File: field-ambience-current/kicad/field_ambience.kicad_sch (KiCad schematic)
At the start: 0 parts

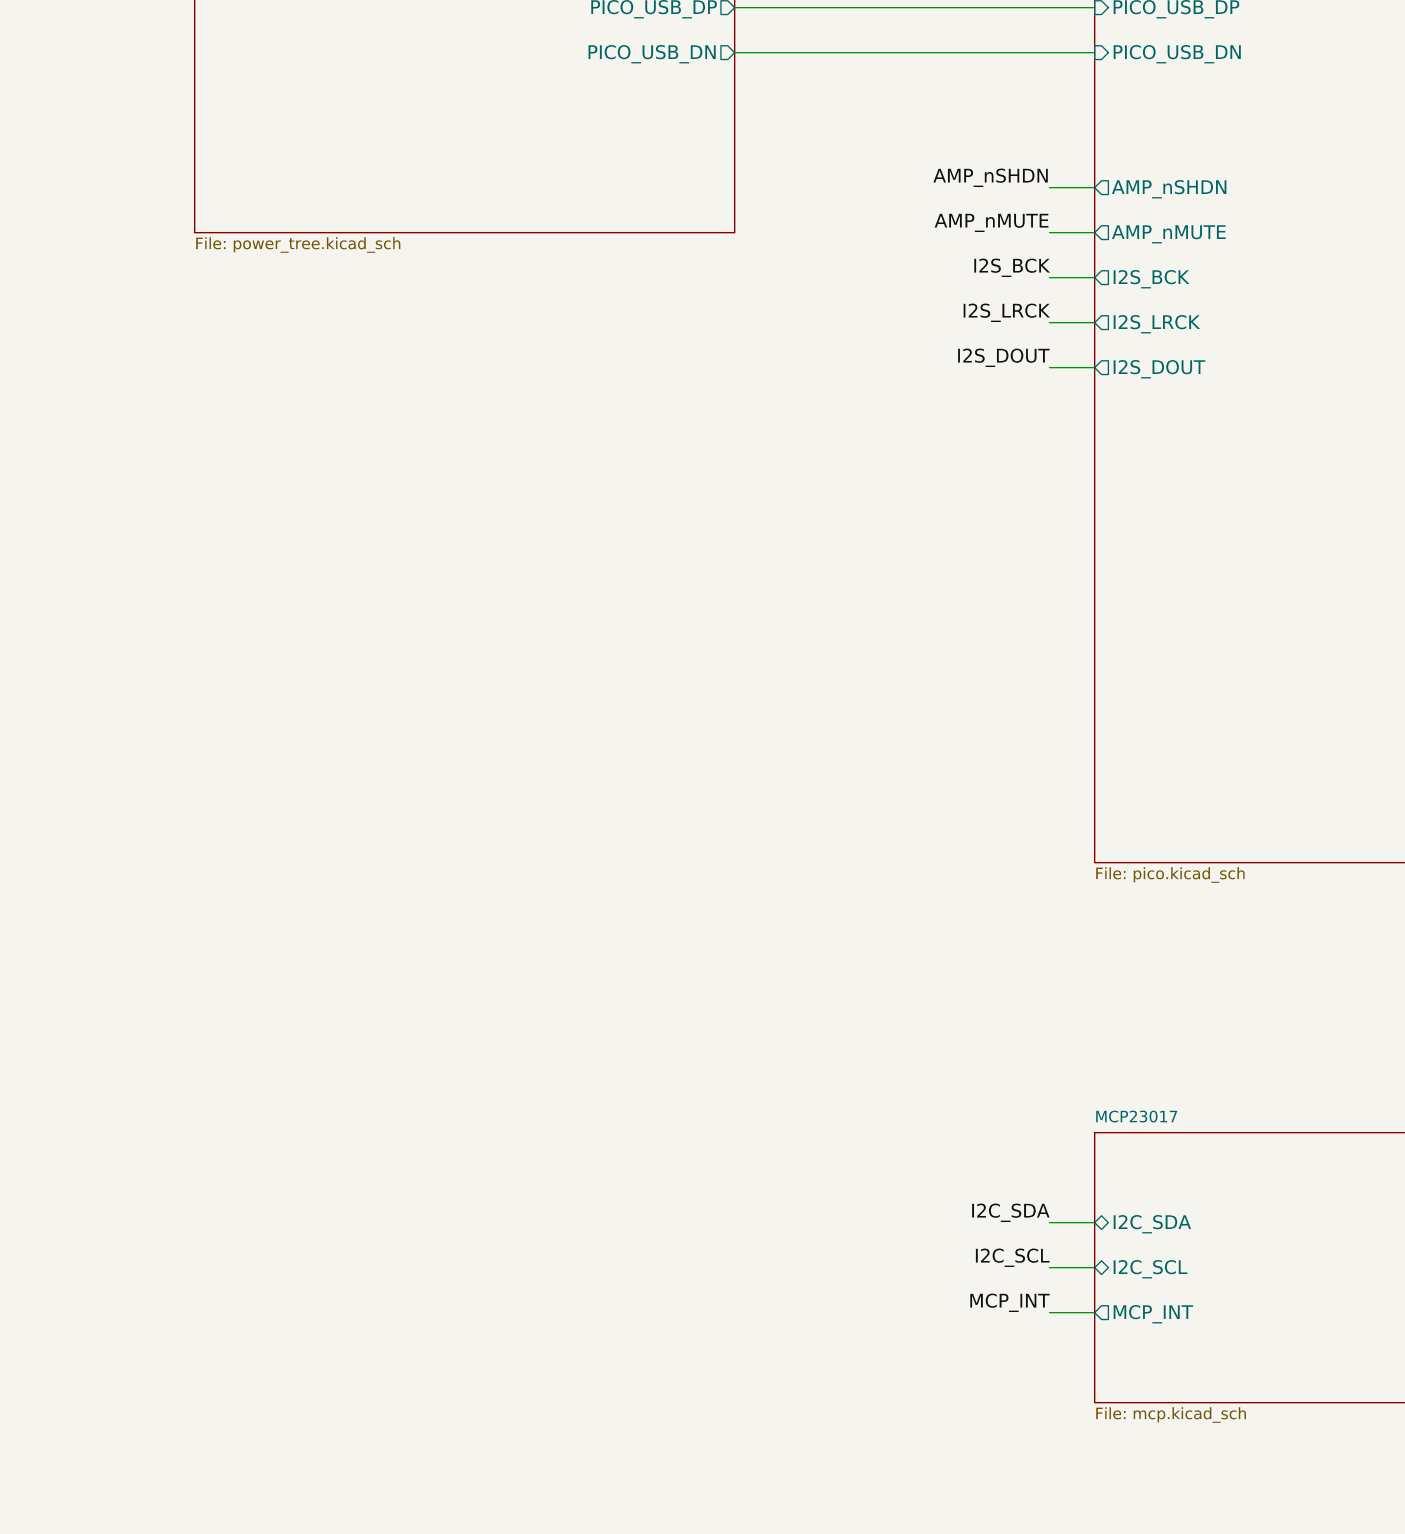
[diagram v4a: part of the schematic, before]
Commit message: pcb(gen): r12-Sense + r9-Battery — KiCad-Generator vervollständigt
Zweite + dritte Hälfte von r10-B9/r7-B3. Bringt Generator vollständig in
Sync mit allen SPEC-Revisionen r9 (Battery-Add), r12 (Battery-Sense-HW),
r10-LED (LED1 auf PCA-Ch 10).

5 neue Library-Symbole (zwischen _pca9685pw_lib_symbol und
_rotary_encoder_switch_lib_symbol):
- _mcp73831_lib_symbol() — SOT-23-5, 5-pin Microchip-Charger
- _tps61089_lib_symbol() — QFN-12+ePAD, 13-pin TI-Boost
- _dmg2305ux_lib_symbol() — SOT-23, 3-pin P-MOSFET
- _inductor_lib_symbol() — Device:L, 2-pin
- _schottky_diode_lib_symbol() — Device:D_Schottky, 2-pin

Neuer Sheet 7 battery.kicad_sch (106 KB, 1848 Zeilen, paren-balanced):
- U7 MCP73831 LiPo-Charger 500mA via R21=2kΩ R_PROG, STAT→R_CHRG→LED_CHRG→+5V
- U8 TPS61089 Boost LiPo→5V mit L1 2.2µH + R23/R24 FB-Divider (200k/39k → ~4.92V)
- Q1 DMG2305UX P-MOS Power-Path (S=VBUS_USBC, D=+5V_OUT, G→R22 10kΩ pull-down)
- D3 SS34 Schottky zwischen BOOST_OUT und +5V_OUT (Reverse-Protect)
- J9 JST-PH-2P, C_BAT_IN/HF (22µF+100nF), C_BOOST_OUT/HF (22µF+100nF)
- Hier-I/O: VBUS_USBC ← (Power-Tree), BAT_PLUS → (Pico), +5V_OUT → (System-Rail)

r12-Sense in pico_sheet:
- GP26 STATUS_LED-Block entfernt (R19+LED1+GND-Flag weg, 0 hits in pico.kicad_sch)
- BAT_SENSE-Divider rein: R_BAT_DIV_TOP/BOT (100kΩ je), C_BAT_FILT (10nF)
- Hier-Input BAT_PLUS am Divider-Top

r12-Sense in mcp_sheet:
- GPA7 NC_GPA7 → USB_VBUS_SENSE mit R_VBUS_SENSE (10kΩ Series) + R_VBUS_PD
  (100kΩ Pull-Down) + hier-Input VBUS_USBC
- LED1 + R_LED_STATUS (390Ω 0603) auf PCA-Ch 10 (Pin 17, rechts) bei (130, 230)
- STATUS_LED_K Net-Label matched LED1-Kathode mit PCA-LED10-Pin
- NC-Loop reduziert auf LED11-LED15

power_tree_sheet:
- VBUS_USBC hier-Output (90° nach oben) am pre-fuse Rail-Tap bei (30.48, RAIL_Y-6)

root_sheet:
- Sheet 7 Battery-Block bei (30, 180) size 60×40 mit Pins VBUS_USBC/BAT_PLUS/+5V_OUT
- Existing Sheet-Blöcke erweitert: power_tree +VBUS_USBC out (90,95), pico +BAT_PLUS
  in (130,165), mcp +VBUS_USBC in 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
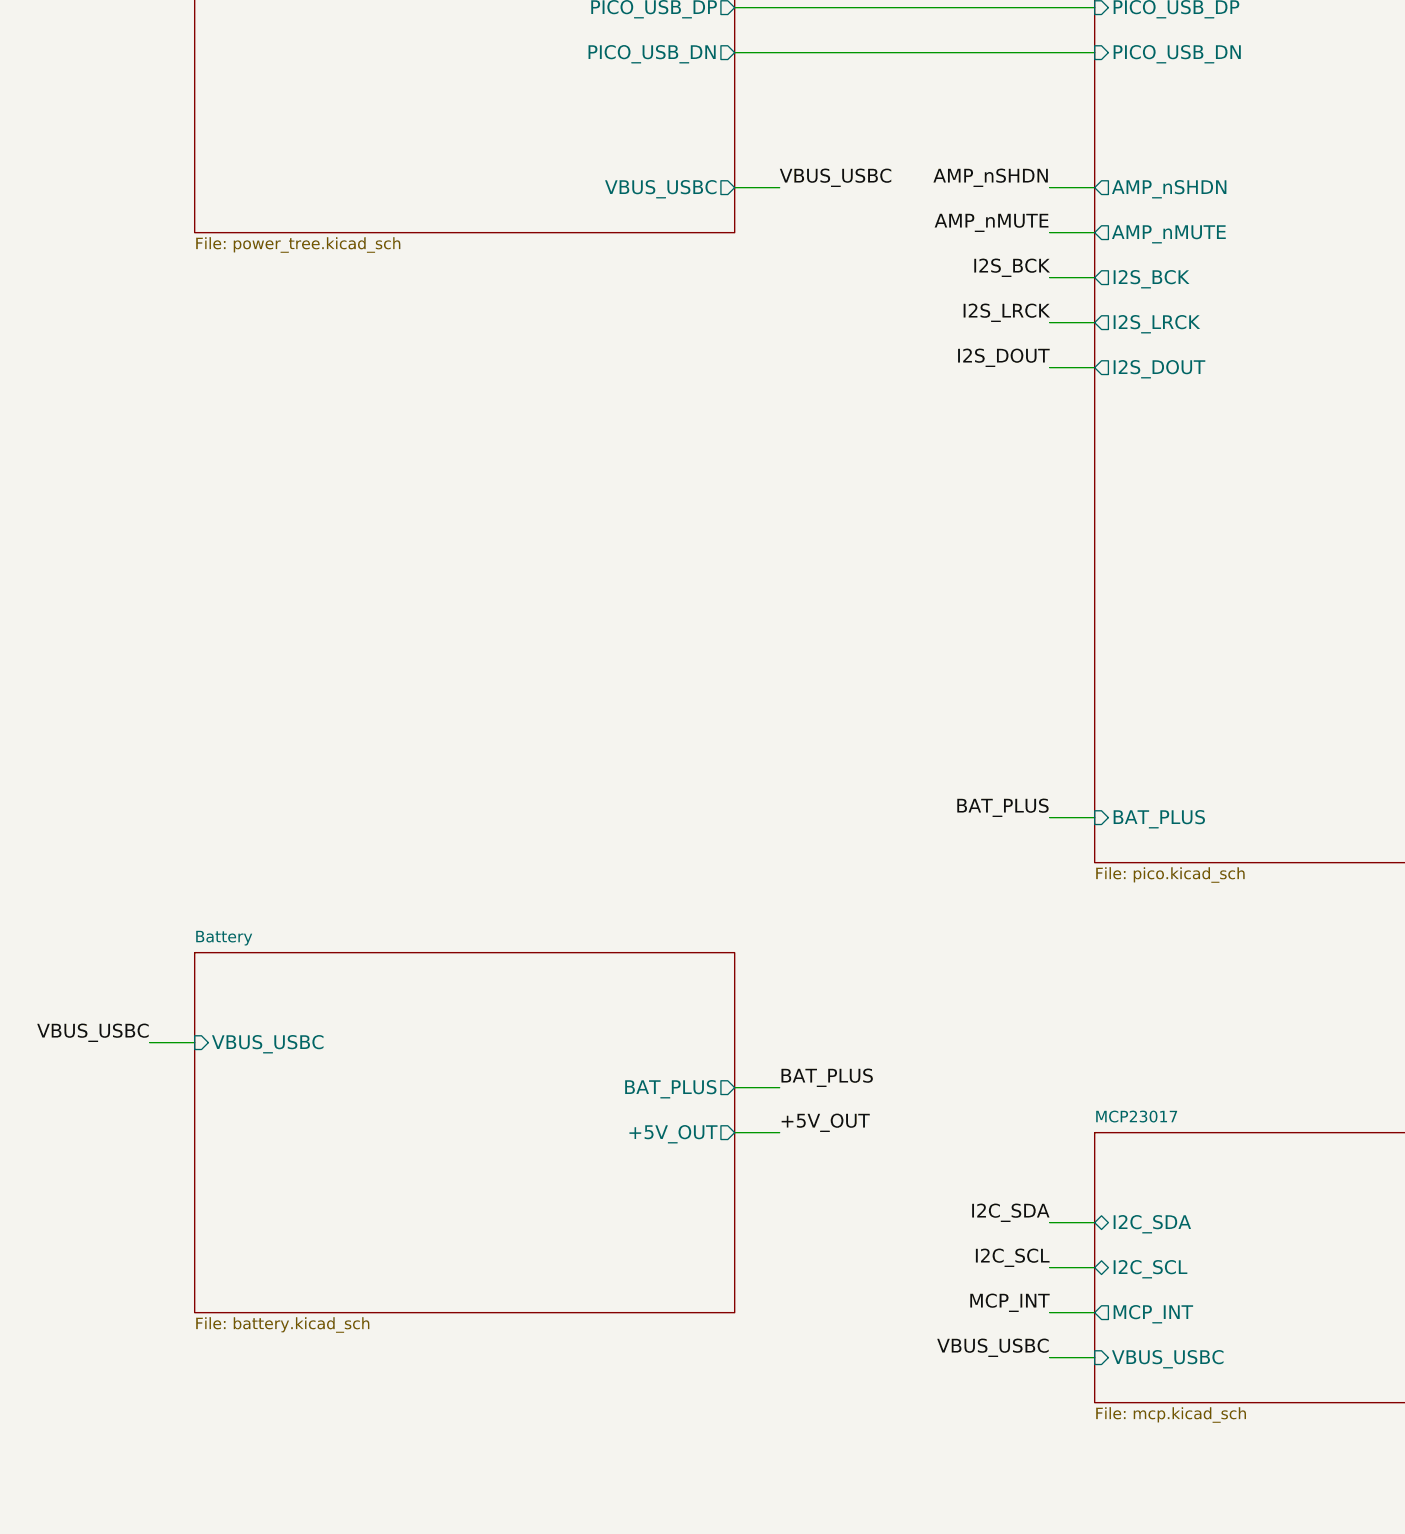
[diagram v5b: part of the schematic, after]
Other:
- added sheet Battery (battery.kicad_sch)
- sheet MCP23017 ports: added VBUS_USBC; removed none
- sheet Pico ports: added BAT_PLUS; removed none
- sheet PowerTree ports: added VBUS_USBC; removed none
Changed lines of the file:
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@@
     (pin "PICO_USB_DN" output (at 90 80 0)
       (effects (font (size 1.524 1.524)) (justify right))
+)
+    (pin "VBUS_USBC" output (at 90 95 0)
+      (effects (font (size 1.524 1.524)) (justify right))
 ))
   (sheet (at 130 40) (size 60 130) (fields_autoplaced)
@@
     (pin "I2S_DOUT" output (at 130 115 180)
       (effects (font (size 1.524 1.524)) (justify left))
+)
+    (pin "BAT_PLUS" input (at 130 165 180)
+      (effects (font (size 1.524 1.524)) (justify left))
 ))
   (sheet (at 230 40) (size 60 60) (fields_autoplaced)
@@
     (pin "JACK_DETECT" input (at 190 210 0)
       (effects (font (size 1.524 1.524)) (justify right))
+)
+    (pin "VBUS_USBC" input (at 130 225 180)
+      (effects (font (size 1.524 1.524)) (justify left))
 ))
   (sheet (at 230 105) (size 60 70) (fields_autoplaced)
@@
       (effects (font (size 1.524 1.524)) (justify left))
 ))
+  (sheet (at 30 180) (size 60 40) (fields_autoplaced)
+    (stroke (width 0.1524) (type solid))
+    (fill (color 0 0 0 0.0000))
+    (property "Sheetname" "Battery" (at 30 179 0)
+      (effects (font (size 1.27 1.27)) (justify left bottom)))
+    (property "Sheetfile" "battery.kicad_sch" (at 30 220.5 0)
+      (effects (font (size 1.27 1.27)) (justify left top)))
+    (pin "VBUS_USBC" input (at 30 190 180)
+      (effects (font (size 1.524 1.524)) (justify left))
+)
+    (pin "BAT_PLUS" output (at 90 195 0)
+      (effects (font (size 1.524 1.524)) (justify right))
+)
+    (pin "+5V_OUT" output (at 90 200 0)
+      (effects (font (size 1.524 1.524)) (justify right))
+))
+  (wire (pts (xy 90 95) (xy 95 95)) (stroke (width 0) (type default)))
+  (label "VBUS_USBC" (at 95 95 0) (effects (font (size 1.524 1.524)) (justify left bottom)))
+  (wire (pts (xy 25 190) (xy 30 190)) (stroke (width 0) (type default)))
+  (label "VBUS_USBC" (at 25 190 0) (effects (font (size 1.524 1.524)) (justify right bottom)))
+  (wire (pts (xy 125 225) (xy 130 225)) (stroke (width 0) (type default)))
+  (label "VBUS_USBC" (at 125 225 0) (effects (font (size 1.524 1.524)) (justify right bottom)))
+  (wire (pts (xy 90 195) (xy 95 195)) (stroke (width 0) (type default)))
+  (label "BAT_PLUS" (at 95 195 0) (effects (font (size 1.524 1.524)) (justify left bottom)))
+  (wire (pts (xy 125 165) (xy 130 165)) (stroke (width 0) (type default)))
+  (label "BAT_PLUS" (at 125 165 0) (effects (font (size 1.524 1.524)) (justify right bottom)))
+  (wire (pts (xy 90 200) (xy 95 200)) (stroke (width 0) (type default)))
+  (label "+5V_OUT" (at 95 200 0) (effects (font (size 1.524 1.524)) (justify left bottom)))
   (wire (pts (xy 125 95) (xy 130 95)) (stroke (width 0) (type default)))
   (label "AMP_nSHDN" (at 125 95 0) (effects (font (size 1.524 1.524)) (justify right bottom)))

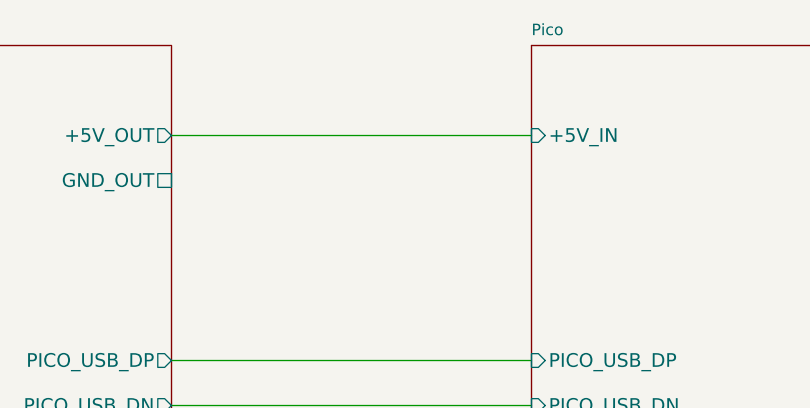
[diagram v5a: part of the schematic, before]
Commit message: pcb(gen): kicad-Analyzer-Bugfixes (ERC: 8 errors→6, NT-001 33→16)
Schematic-Analyzer fand drei klassen von echten Connectivity-Bugs in den
beiden Generator-Catchup-Commits (50b5e02 + 0a3a740). Alle gefixt.

Bug 1: Label-Position 3mm neben Wire-Endpunkt → 33 dangling-pin-Nets
  - r10-LED PCA-pin-Labels (10 LEDs + 5 NC + STATUS_LED_K) saßen bei
    PCA_PIN_*_X±8 statt ±5 → keine 10 LEDs waren physisch an PCA9685
    connected. Fix: Labels auf Wire-Endpunkt verschoben.

Bug 2: Sub-mm-Gaps (0.19mm) zwischen Wires und Resistor-Pins
  - R rotation=90 horizontal hat pin1/pin2 bei sx±3.81 (X.19/X.81).
    Meine Wires endeten bei integer-mm → 0.19mm Gap = dangling.
  - Fixed: R_OE (mcp_sheet PCA-OE), R_VBUS_SENSE (mcp_sheet GPA7),
    R_CHRG (battery_sheet U7-STAT), R21 (battery_sheet U7-PROG).

Bug 3: Y-Inversion bei Q1 DMG2305UX P-MOS
  - KiCad-Symbol-local-Y ist invertiert zu Schematic-abs-Y. Meine
    q1_s_y und q1_d_y waren vertauscht → Q1.2 (S) auf +5V_OUT statt
    VBUS_USBC (SPEC-§2.2-violation!). Analyzer hat das korrekt
    gefangen. Fix: Y-Werte getauscht, S=VBUS_USBC ✓, D=+5V_OUT ✓.

Bug 4: Lokal-Label statt Hier-Label für Cross-Sheet-Nets
  - Lokale Labels mergen NICHT mit Hier-Labels im Analyzer-View
    (auch wenn KiCad-GUI das toleriert). Battery_sheet U7-VDD,
    U7-VBAT, U8-VIN, L1-top, Q1-D, D3-K, J9-pin1, C_BAT_IN waren
    alle mit lokalen Labels markiert → keine Cross-Sheet-Merge.
    Plus mcp_sheet PCA-side I²C-SCL/SDA.
  - Fix: alle zu hier_labels umgewandelt. I²C-Bus hat jetzt 4 Pins
    (U1+U2+R-Pullup+U6) statt 2 isolierte Sub-Nets.

Bug 5: +5V_OUT (Battery) mergt nicht mit System +5V
  - Hier-Label-Name "+5V_OUT" ≠ Power-Tree-Net-Name "+5V". Battery's
    +5V_OUT war ein isoliertes 2-pin Net (D3.K + Q1.D).
  - Fix: Bridge-Label "+5V_OUT" am existing Power-Tree→Pico-Wire
    (110, 50) im root_sheet. +5V hat jetzt 49 pins (war 47).

Bug 6: Redundante Edge-Hier-Labels in battery_sheet
  - Hatte standalone hier_labels bei (235, 70/80) zusätzlich zu de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
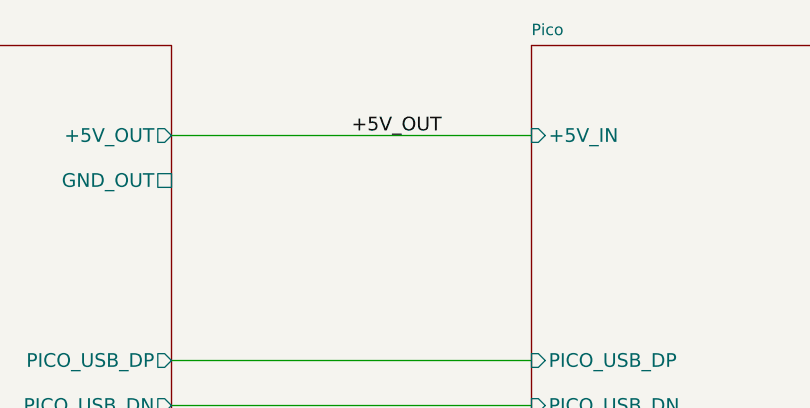
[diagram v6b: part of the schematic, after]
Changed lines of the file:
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@@
   (wire (pts (xy 90 200) (xy 95 200)) (stroke (width 0) (type default)))
   (label "+5V_OUT" (at 95 200 0) (effects (font (size 1.524 1.524)) (justify left bottom)))
+  (label "+5V_OUT" (at 110 50 0) (effects (font (size 1.524 1.524)) (justify left bottom)))
   (wire (pts (xy 125 95) (xy 130 95)) (stroke (width 0) (type default)))
   (label "AMP_nSHDN" (at 125 95 0) (effects (font (size 1.524 1.524)) (justify right bottom)))
